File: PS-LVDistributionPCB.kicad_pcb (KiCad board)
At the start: 2 copper layers, 226 x 70 mm, 81 parts, among them J1 CRIT OUT, J10 NON CRIT OUT, J11 NON CRIT OUT, J12 NON CRIT OUT, J13 NON CRIT OUT, J14 NON CRIT OUT, J15 NON CRIT OUT, J16 NON CRIT OUT, J17 NON CRIT OUT, J18 NON CRIT OUT, J19 NON CRIT OUT, J2 CRIT OUT, J20 CRIT, J21 NON CRIT, J3 CRIT OUT, J4 CRIT OUT, J5 CRIT OUT, J6 CRIT OUT, J7 CRIT OUT, J8 NON CRIT OUT, J9 NON CRIT OUT

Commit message: Added optoisolators to ensure LED indicators are powered by critical power and only turn on when the fuse blows. Fuses and resistors on the back for waterproofing.
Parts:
- removed D1, D10, D11, D12, D13, D14, D15, D16, D17, D18, D19, D2, D3, D4, D5, D6, D7, D8, D9: 20mA, LED_SMD:LED_0805_2012Metric
- removed F1, F10, F11, F12, F13, F14, F15, F16, F17, F18, F19, F2, F3, F4, F5, F6, F7, F8, F9: 10A, footprints:3588
- removed F20, F21: 30A, footprints:3588
- removed the G*** at (216.6, 85.2)
- removed J1, J2, J3, J4, J5, J6, J7: CRIT OUT, footprints:Molex_Micro-Fit_3.0_43650-0215_1x02_P3.00mm_Vertical
- removed J10, J11, J12, J13, J14, J15, J16, J17, J18, J19, J8, J9: NON CRIT OUT, footprints:Molex_Micro-Fit_3.0_43650-0215_1x02_P3.00mm_Vertical
- removed J20: CRIT, Connector_Molex:Molex_Sabre_43160-0102_1x02_P7.49mm_Vertical
- removed J21: NON CRIT, Connector_Molex:Molex_Sabre_43160-0102_1x02_P7.49mm_Vertical
- removed R1, R10, R11, R12, R13, R14, R15, R16, R17, R18, R19, R2, R3, R4, R5, R6, R7, R8, R9: 1k, Resistor_SMD:R_0805_2012Metric
- added C_D1: 20mA, LED_SMD:LED_0805_2012Metric, F.Cu at (92.0, 89.1)
- added C_D2: 20mA, LED_SMD:LED_0805_2012Metric, F.Cu at (108.4, 89.2)
- added C_D3: 20mA, LED_SMD:LED_0805_2012Metric, F.Cu at (124.9, 89.2)
- added C_D4: 20mA, LED_SMD:LED_0805_2012Metric, F.Cu at (140.9, 89.2)
- added C_D5: 20mA, LED_SMD:LED_0805_2012Metric, F.Cu at (157.1, 89.1)
- added C_D6: 20mA, LED_SMD:LED_0805_2012Metric, F.Cu at (173.1, 89.1)
- added C_D7: 20mA, LED_SMD:LED_0805_2012Metric, F.Cu at (189.4, 89.2)
- added C_F1: 10A, footprints:3588, B.Cu at (92.0, 73.6)
- added C_F2: 10A, footprints:3588, B.Cu at (108.4, 73.6)
- added C_F3: 10A, footprints:3588, B.Cu at (124.9, 73.6)
- added C_F4: 10A, footprints:3588, B.Cu at (140.9, 73.7)
- added C_F5: 10A, footprints:3588, B.Cu at (157.1, 73.6)
- added C_F6: 10A, footprints:3588, B.Cu at (173.1, 73.6)
- added C_F7: 10A, footprints:3588, B.Cu at (189.4, 73.7)
- added C_J1: CRIT OUT, footprints:Molex_Micro-Fit_3.0_43650-0215_1x02_P3.00mm_Vertical, F.Cu at (90.5, 94.7)
- added C_J2: CRIT OUT, footprints:Molex_Micro-Fit_3.0_43650-0215_1x02_P3.00mm_Vertical, F.Cu at (106.9, 94.7)
- added C_J3: CRIT OUT, footprints:Molex_Micro-Fit_3.0_43650-0215_1x02_P3.00mm_Vertical, F.Cu at (123.4, 94.7)
- added C_J4: CRIT OUT, footprints:Molex_Micro-Fit_3.0_43650-0215_1x02_P3.00mm_Vertical, F.Cu at (139.4, 94.8)
- added C_J5: CRIT OUT, footprints:Molex_Micro-Fit_3.0_43650-0215_1x02_P3.00mm_Vertical, F.Cu at (155.6, 94.7)
- added C_J6: CRIT OUT, footprints:Molex_Micro-Fit_3.0_43650-0215_1x02_P3.00mm_Vertical, F.Cu at (171.6, 94.7)
- added C_J7: CRIT OUT, footprints:Molex_Micro-Fit_3.0_43650-0215_1x02_P3.00mm_Vertical, F.Cu at (187.9, 94.8)
- added C_R1: 105, Resistor_SMD:R_0805_2012Metric, B.Cu at (86.6, 84.7)
- added C_R10: 1k, Resistor_SMD:R_0805_2012Metric, B.Cu at (162.6, 84.6)
- added C_R11: 105, Resistor_SMD:R_0805_2012Metric, B.Cu at (167.6, 84.7)
- added C_R12: 1k, Resistor_SMD:R_0805_2012Metric, B.Cu at (178.6, 84.6)
- added C_R13: 105, Resistor_SMD:R_0805_2012Metric, B.Cu at (183.9, 84.8)
- added C_R14: 1k, Resistor_SMD:R_0805_2012Metric, B.Cu at (194.9, 84.7)
- added C_R2: 1k, Resistor_SMD:R_0805_2012Metric, B.Cu at (97.6, 84.6)
- added C_R3: 105, Resistor_SMD:R_0805_2012Metric, B.Cu at (102.9, 84.7)
- added C_R4: 1k, Resistor_SMD:R_0805_2012Metric, B.Cu at (113.9, 84.7)
- added C_R5: 105, Resistor_SMD:R_0805_2012Metric, B.Cu at (119.4, 84.7)
- added C_R6: 1k, Resistor_SMD:R_0805_2012Metric, B.Cu at (130.4, 84.7)
- added C_R7: 105, Resistor_SMD:R_0805_2012Metric, B.Cu at (135.4, 84.8)
- added C_R8: 1k, Resistor_SMD:R_0805_2012Metric, B.Cu at (146.4, 84.7)
- added C_R9: 105, Resistor_SMD:R_0805_2012Metric, B.Cu at (151.6, 84.7)
- added C_U1: EL3H7, Package_SO:SOP-4_4.4x2.6mm_P1.27mm, B.Cu at (92.0, 84.6)
- added C_U2: EL3H7, Package_SO:SOP-4_4.4x2.6mm_P1.27mm, B.Cu at (108.4, 84.7)
- added C_U3: EL3H7, Package_SO:SOP-4_4.4x2.6mm_P1.27mm, B.Cu at (124.9, 84.7)
- added C_U4: EL3H7, Package_SO:SOP-4_4.4x2.6mm_P1.27mm, B.Cu at (140.9, 84.7)
- added C_U5: EL3H7, Package_SO:SOP-4_4.4x2.6mm_P1.27mm, B.Cu at (157.1, 84.6)
- added C_U6: EL3H7, Package_SO:SOP-4_4.4x2.6mm_P1.27mm, B.Cu at (173.1, 84.6)
- added C_U7: EL3H7, Package_SO:SOP-4_4.4x2.6mm_P1.27mm, B.Cu at (189.4, 84.7)
- added G***: LOGO, UTSVT Connectors:UTSVTsmall, B.Cu at (204.6, 72.0)
- added IN_F1: 30A, footprints:3588, B.Cu at (75.6, 70.4)
- added IN_F2: 30A, footprints:3588, B.Cu at (75.6, 129.4)
- added IN_J1: CRIT, Connector_Molex:Molex_Sabre_43160-0102_1x02_P7.49mm_Vertical, B.Cu at (71.9, 91.9)
- added IN_J2: NON CRIT, Connector_Molex:Molex_Sabre_43160-0102_1x02_P7.49mm_Vertical, B.Cu at (71.9, 114.9)
- added NC_D1: 20mA, LED_SMD:LED_0805_2012Metric, F.Cu at (92.1, 110.6)
- added NC_D10: 20mA, LED_SMD:LED_0805_2012Metric, F.Cu at (238.6, 110.4)
- added NC_D11: 20mA, LED_SMD:LED_0805_2012Metric, F.Cu at (238.6, 89.4)
- added NC_D12: 20mA, LED_SMD:LED_0805_2012Metric, F.Cu at (222.1, 89.4)
- added NC_D2: 20mA, LED_SMD:LED_0805_2012Metric, F.Cu at (108.4, 110.6)
- added NC_D3: 20mA, LED_SMD:LED_0805_2012Metric, F.Cu at (124.9, 110.6)
- added NC_D4: 20mA, LED_SMD:LED_0805_2012Metric, F.Cu at (140.9, 110.6)
- added NC_D5: 20mA, LED_SMD:LED_0805_2012Metric, F.Cu at (156.9, 110.6)
- added NC_D6: 20mA, LED_SMD:LED_0805_2012Metric, F.Cu at (172.9, 110.5)
- added NC_D7: 20mA, LED_SMD:LED_0805_2012Metric, F.Cu at (189.4, 110.6)
- added NC_D8: 20mA, LED_SMD:LED_0805_2012Metric, F.Cu at (205.6, 110.3)
- added NC_D9: 20mA, LED_SMD:LED_0805_2012Metric, F.Cu at (222.1, 110.4)
- added NC_F1: 10A, footprints:3588, B.Cu at (92.0, 125.6)
- added NC_F10: 10A, footprints:3588, B.Cu at (238.5, 125.4)
- added NC_F11: 10A, footprints:3588, B.Cu at (238.6, 73.7)
- added NC_F12: 10A, footprints:3588, B.Cu at (222.1, 73.7)
- added NC_F2: 10A, footprints:3588, B.Cu at (108.4, 125.6)
- added NC_F3: 10A, footprints:3588, B.Cu at (124.9, 125.6)
- added NC_F4: 10A, footprints:3588, B.Cu at (140.9, 125.6)
- added NC_F5: 10A, footprints:3588, B.Cu at (156.9, 125.6)
- added NC_F6: 10A, footprints:3588, B.Cu at (172.9, 125.5)
- added NC_F7: 10A, footprints:3588, B.Cu at (189.4, 125.6)
- added NC_F8: 10A, footprints:3588, B.Cu at (205.5, 125.3)
- added NC_F9: 10A, footprints:3588, B.Cu at (222.1, 125.4)
- added NC_J1: NON CRIT OUT, footprints:Molex_Micro-Fit_3.0_43650-0215_1x02_P3.00mm_Vertical, F.Cu at (93.6, 105.1)
- added NC_J10: NON CRIT OUT, footprints:Molex_Micro-Fit_3.0_43650-0215_1x02_P3.00mm_Vertical, F.Cu at (240.1, 104.9)
- added NC_J11: NON CRIT OUT, footprints:Molex_Micro-Fit_3.0_43650-0215_1x02_P3.00mm_Vertical, F.Cu at (237.1, 94.9)
- added NC_J12: NON CRIT OUT, footprints:Molex_Micro-Fit_3.0_43650-0215_1x02_P3.00mm_Vertical, F.Cu at (220.6, 94.9)
- added NC_J2: NON CRIT OUT, footprints:Molex_Micro-Fit_3.0_43650-0215_1x02_P3.00mm_Vertical, F.Cu at (109.9, 105.1)
- added NC_J3: NON CRIT OUT, footprints:Molex_Micro-Fit_3.0_43650-0215_1x02_P3.00mm_Vertical, F.Cu at (126.4, 105.1)
- added NC_J4: NON CRIT OUT, footprints:Molex_Micro-Fit_3.0_43650-0215_1x02_P3.00mm_Vertical, F.Cu at (142.4, 105.1)
- added NC_J5: NON CRIT OUT, footprints:Molex_Micro-Fit_3.0_43650-0215_1x02_P3.00mm_Vertical, F.Cu at (158.4, 105.1)
- added NC_J6: NON CRIT OUT, footprints:Molex_Micro-Fit_3.0_43650-0215_1x02_P3.00mm_Vertical, F.Cu at (174.4, 105.0)
- added NC_J7: NON CRIT OUT, footprints:Molex_Micro-Fit_3.0_43650-0215_1x02_P3.00mm_Vertical, F.Cu at (190.9, 105.1)
- added NC_J8: NON CRIT OUT, footprints:Molex_Micro-Fit_3.0_43650-0215_1x02_P3.00mm_Vertical, F.Cu at (207.1, 104.8)
- added NC_J9: NON CRIT OUT, footprints:Molex_Micro-Fit_3.0_43650-0215_1x02_P3.00mm_Vertical, F.Cu at (223.6, 104.9)
- added NC_R1: 105, Resistor_SMD:R_0805_2012Metric, B.Cu at (97.6, 114.7)
- added NC_R10: 1k, Resistor_SMD:R_0805_2012Metric, B.Cu at (151.4, 114.7)
- added NC_R11: 105, Resistor_SMD:R_0805_2012Metric, B.Cu at (178.4, 114.6)
- added NC_R12: 1k, Resistor_SMD:R_0805_2012Metric, B.Cu at (167.4, 114.6)
- added NC_R13: 105, Resistor_SMD:R_0805_2012Metric, B.Cu at (194.9, 114.7)
- added NC_R14: 1k, Resistor_SMD:R_0805_2012Metric, B.Cu at (183.9, 114.7)
- added NC_R15: 105, Resistor_SMD:R_0805_2012Metric, B.Cu at (211.1, 114.4)
- added NC_R16: 1k, Resistor_SMD:R_0805_2012Metric, B.Cu at (200.1, 114.4)
- added NC_R17: 105, Resistor_SMD:R_0805_2012Metric, B.Cu at (227.6, 114.5)
- added NC_R18: 1k, Resistor_SMD:R_0805_2012Metric, B.Cu at (216.6, 114.5)
- added NC_R19: 105, Resistor_SMD:R_0805_2012Metric, B.Cu at (244.1, 114.5)
- added NC_R2: 1k, Resistor_SMD:R_0805_2012Metric, B.Cu at (86.6, 114.7)
- added NC_R20: 1k, Resistor_SMD:R_0805_2012Metric, B.Cu at (233.1, 114.5)
- added NC_R21: 105, Resistor_SMD:R_0805_2012Metric, B.Cu at (233.1, 84.7)
- added NC_R22: 1k, Resistor_SMD:R_0805_2012Metric, B.Cu at (244.1, 84.7)
- added NC_R23: 105, Resistor_SMD:R_0805_2012Metric, B.Cu at (216.6, 84.7)
- added NC_R24: 1k, Resistor_SMD:R_0805_2012Metric, B.Cu at (227.6, 84.7)
- added NC_R3: 105, Resistor_SMD:R_0805_2012Metric, B.Cu at (113.9, 114.7)
- added NC_R4: 1k, Resistor_SMD:R_0805_2012Metric, B.Cu at (102.9, 114.7)
- added NC_R5: 105, Resistor_SMD:R_0805_2012Metric, B.Cu at (130.4, 114.7)
- added NC_R6: 1k, Resistor_SMD:R_0805_2012Metric, B.Cu at (119.4, 114.7)
- added NC_R7: 105, Resistor_SMD:R_0805_2012Metric, B.Cu at (146.4, 114.7)
- added NC_R8: 1k, Resistor_SMD:R_0805_2012Metric, B.Cu at (135.4, 114.7)
- added NC_R9: 105, Resistor_SMD:R_0805_2012Metric, B.Cu at (162.4, 114.7)
- added NC_U1: EL3H7, Package_SO:SOP-4_4.4x2.6mm_P1.27mm, B.Cu at (92.1, 114.7)
- added NC_U10: EL3H7, Package_SO:SOP-4_4.4x2.6mm_P1.27mm, B.Cu at (238.6, 114.5)
- added NC_U11: EL3H7, Package_SO:SOP-4_4.4x2.6mm_P1.27mm, B.Cu at (238.6, 84.7)
- added NC_U12: EL3H7, Package_SO:SOP-4_4.4x2.6mm_P1.27mm, B.Cu at (222.1, 84.7)
- added NC_U2: EL3H7, Package_SO:SOP-4_4.4x2.6mm_P1.27mm, B.Cu at (108.4, 114.7)
- added NC_U3: EL3H7, Package_SO:SOP-4_4.4x2.6mm_P1.27mm, B.Cu at (124.9, 114.7)
- added NC_U4: EL3H7, Package_SO:SOP-4_4.4x2.6mm_P1.27mm, B.Cu at (140.9, 114.7)
- added NC_U5: EL3H7, Package_SO:SOP-4_4.4x2.6mm_P1.27mm, B.Cu at (156.9, 114.7)
- added NC_U6: EL3H7, Package_SO:SOP-4_4.4x2.6mm_P1.27mm, B.Cu at (172.9, 114.6)
- added NC_U7: EL3H7, Package_SO:SOP-4_4.4x2.6mm_P1.27mm, B.Cu at (189.4, 114.7)
- added NC_U8: EL3H7, Package_SO:SOP-4_4.4x2.6mm_P1.27mm, B.Cu at (205.6, 114.4)
- added NC_U9: EL3H7, Package_SO:SOP-4_4.4x2.6mm_P1.27mm, B.Cu at (222.1, 114.5)
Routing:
- net GND: track 0.00 -> 178.5 mm, vias 0 -> 19
- net +12V_NON: track 72.7 -> 7.36 mm
- net +12V CRIT: track 42.4 -> 0.00 mm
- net Net-(NC_D10-A): track 0.00 -> 13.1 mm, vias 0 -> 1
- net Net-(NC_D9-A): track 0.00 -> 13.1 mm, vias 0 -> 1
- net Net-(NC_D7-A): track 0.00 -> 13.1 mm, vias 0 -> 1
- net Net-(NC_D6-A): track 0.00 -> 13.1 mm, vias 0 -> 1
- net Net-(NC_D5-A): track 0.00 -> 13.1 mm, vias 0 -> 1
- net Net-(NC_D2-A): track 0.00 -> 13.1 mm, vias 0 -> 1
- net Net-(NC_D8-A): track 0.00 -> 13.1 mm, vias 0 -> 1
- net Net-(NC_D4-A): track 0.00 -> 13.1 mm, vias 0 -> 1
- net Net-(NC_D3-A): track 0.00 -> 13.1 mm, vias 0 -> 1
- net Net-(NC_D12-A): track 0.00 -> 7.27 mm, vias 0 -> 1
- net Net-(NC_D11-A): track 0.00 -> 7.27 mm, vias 0 -> 1
- net Net-(C_D6-A): track 0.00 -> 7.25 mm, vias 0 -> 1
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- added copper zone on B.Cu, net Net-(C_J1-Pin_1)
- added copper zone on B.Cu, net Net-(C_J2-Pin_1)
- added copper zone on B.Cu, net Net-(C_J3-Pin_1)
- added copper zone on B.Cu, net Net-(C_J4-Pin_1)
- added copper zone on B.Cu, net Net-(C_J5-Pin_1)
- added copper zone on B.Cu, net Net-(C_J6-Pin_1)
- added copper zone on B.Cu, net Net-(C_J7-Pin_1)
- added copper zone on B.Cu, net Net-(IN_J1-Pin_1)
- added copper zone on B.Cu, net Net-(IN_J2-Pin_1)
- added copper zone on B.Cu, net Net-(NC_J1-Pin_1)
- added copper zone on B.Cu, net Net-(NC_J10-Pin_1)
- added copper zone on B.Cu, net Net-(NC_J11-Pin_1)
- added copper zone on B.Cu, net Net-(NC_J12-Pin_1)
- added copper zone on B.Cu, net Net-(NC_J2-Pin_1)
- added copper zone on B.Cu, net Net-(NC_J3-Pin_1)
- added copper zone on B.Cu, net Net-(NC_J4-Pin_1)
- added copper zone on B.Cu, net Net-(NC_J5-Pin_1)
- added copper zone on B.Cu, net Net-(NC_J6-Pin_1)
- added copper zone on B.Cu, net Net-(NC_J7-Pin_1)
- added copper zone on B.Cu, net Net-(NC_J8-Pin_1)
- added copper zone on B.Cu, net Net-(NC_J9-Pin_1)
- removed copper zone on B.Cu, net Net-(J1-Pin_1)
- removed copper zone on B.Cu, net Net-(J10-Pin_1)
- removed copper zone on B.Cu, net Net-(J11-Pin_1)
- removed copper zone on B.Cu, net Net-(J12-Pin_1)
- removed copper zone on B.Cu, net Net-(J13-Pin_1)
- removed copper zone on B.Cu, net Net-(J14-Pin_1)
- removed copper zone on B.Cu, net Net-(J15-Pin_1)
- removed copper zone on B.Cu, net Net-(J16-Pin_1)
- removed copper zone on B.Cu, net Net-(J17-Pin_1)
- removed copper zone on B.Cu, net Net-(J18-Pin_1)
- removed copper zone on B.Cu, net Net-(J19-Pin_1)
- removed copper zone on B.Cu, net Net-(J2-Pin_1)
- removed copper zone on B.Cu, net Net-(J20-Pin_1)
- removed copper zone on B.Cu, net Net-(J21-Pin_1)
- removed copper zone on B.Cu, net Net-(J3-Pin_1)
- removed copper zone on B.Cu, net Net-(J4-Pin_1)
- removed copper zone on B.Cu, net Net-(J5-Pin_1)
- removed copper zone on B.Cu, net Net-(J6-Pin_1)
- removed copper zone on B.Cu, net Net-(J7-Pin_1)
- removed copper zone on B.Cu, net Net-(J8-Pin_1)
- removed copper zone on B.Cu, net Net-(J9-Pin_1)
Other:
- board size 226 x 70 mm -> 191.9 x 83.9 mm
- board text added: "LV Distribution Surabhi Karighattam 2024"
- board text added: "NON CRIT 1"
- board text added: "NON CRIT 10"
- board text added: "NON CRIT 11"
- board text added: "NON CRIT 12"
- board text added: "NON CRIT 2"
- board text added: "NON CRIT 3"
- board text added: "NON CRIT 4"
- board text added: "NON CRIT 5"
- board text added: "NON CRIT 6"
- board text added: "NON CRIT 7"
- board text added: "NON CRIT 8"
- board text added: "NON CRIT 9"
- board text added: "NON CRIT IN"
- board text removed: "LV Distribution Surabhi Karighattam 2025"
- board text removed: "NC 1"
- board text removed: "NC 10"
- board text removed: "NC 11"
- board text removed: "NC 12"
- board text removed: "NC 2"
- board text removed: "NC 3"
- board text removed: "NC 4"
- board text removed: "NC 5"
- board text removed: "NC 6"
- board text removed: "NC 7"
- board text removed: "NC 8"
- board text removed: "NC 9"
- board text removed: "NC IN"

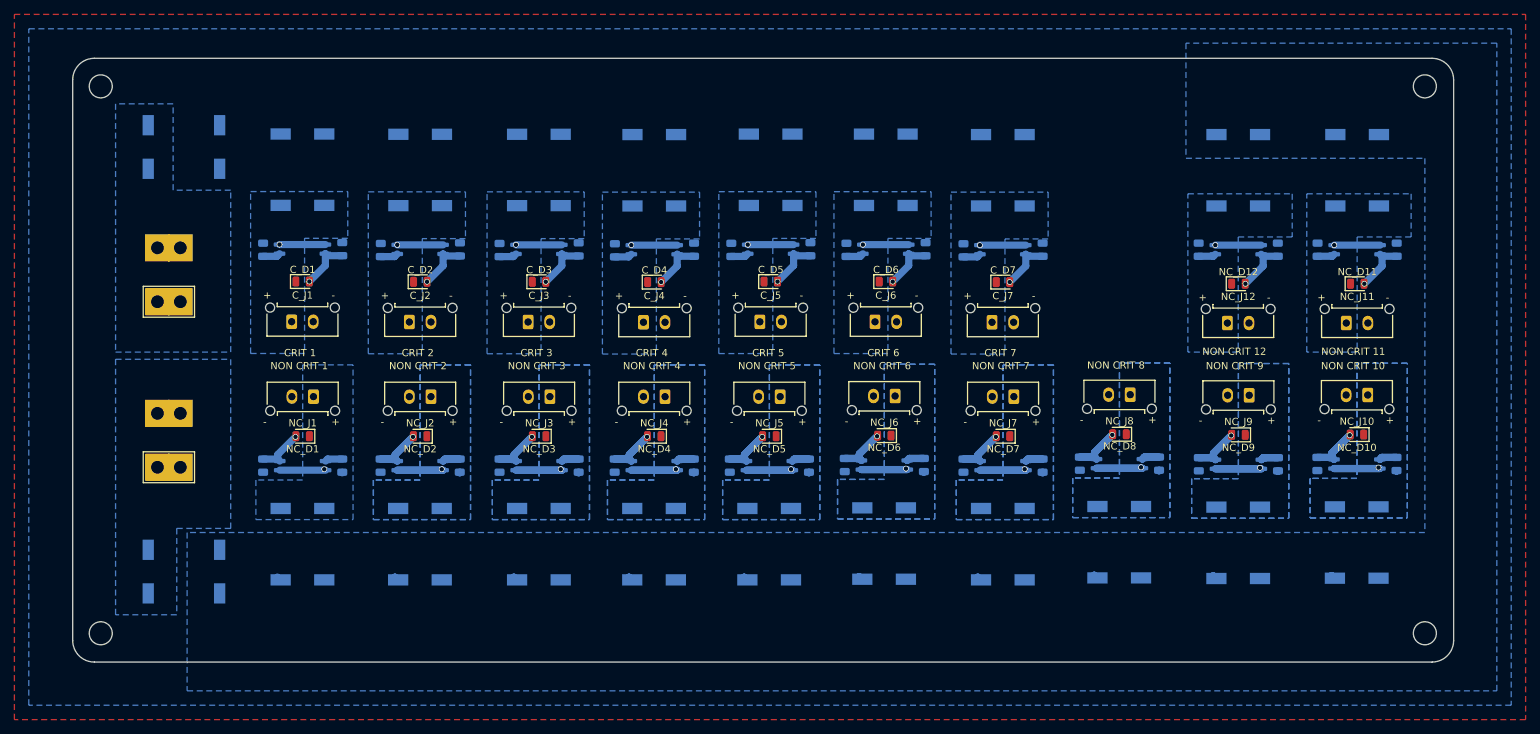
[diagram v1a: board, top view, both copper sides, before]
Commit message: xt30s + right angle mx150 initial layout
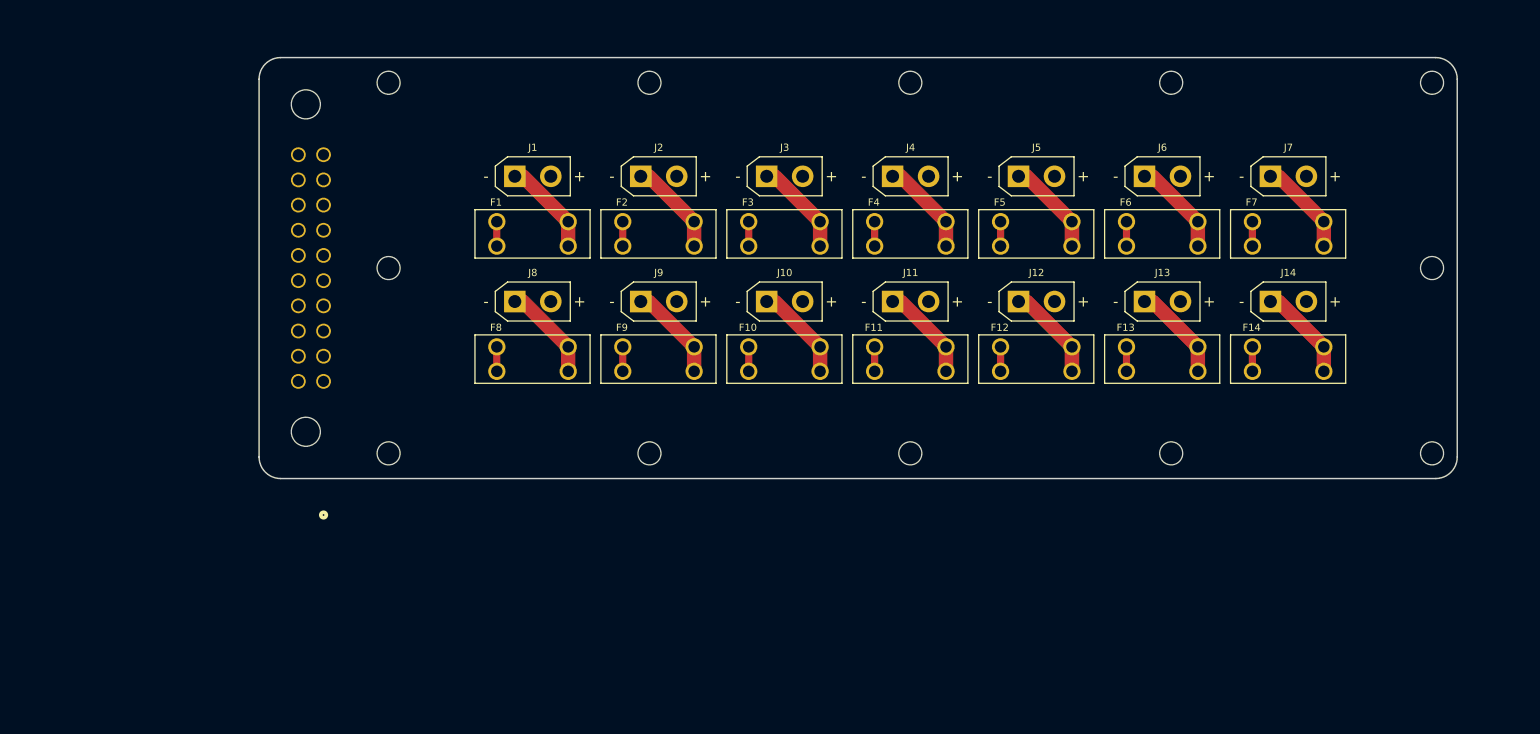
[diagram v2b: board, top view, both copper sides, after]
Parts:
- removed C_D1, C_D2, C_D3, C_D4, C_D5, C_D6, C_D7, NC_D1, NC_D10, NC_D11, NC_D12, NC_D2, NC_D3, NC_D4, NC_D5, NC_D6, NC_D7, NC_D8, NC_D9: 20mA, LED_SMD:LED_0805_2012Metric
- removed C_F1, C_F2, C_F3, C_F4, C_F5, C_F6, C_F7, NC_F1, NC_F10, NC_F11, NC_F12, NC_F2, NC_F3, NC_F4, NC_F5, NC_F6, NC_F7, NC_F8, NC_F9: 10A, footprints:3588
- removed C_J1, C_J2, C_J3, C_J4, C_J5, C_J6, C_J7: CRIT OUT, footprints:Molex_Micro-Fit_3.0_43650-0215_1x02_P3.00mm_Vertical
- removed C_R1, C_R11, C_R13, C_R3, C_R5, C_R7, C_R9, NC_R1, NC_R11, NC_R13, NC_R15, NC_R17, NC_R19, NC_R21, NC_R23, NC_R3, NC_R5, NC_R7, NC_R9: 105, Resistor_SMD:R_0805_2012Metric
- removed C_R10, C_R12, C_R14, C_R2, C_R4, C_R6, C_R8, NC_R10, NC_R12, NC_R14, NC_R16, NC_R18, NC_R2, NC_R20, NC_R22, NC_R24, NC_R4, NC_R6, NC_R8: 1k, Resistor_SMD:R_0805_2012Metric
- removed C_U1, C_U2, C_U3, C_U4, C_U5, C_U6, C_U7, NC_U1, NC_U10, NC_U11, NC_U12, NC_U2, NC_U3, NC_U4, NC_U5, NC_U6, NC_U7, NC_U8, NC_U9: EL3H7, Package_SO:SOP-4_4.4x2.6mm_P1.27mm
- removed G***: LOGO, UTSVT Connectors:UTSVTsmall
- removed IN_F1, IN_F2: 30A, footprints:3588
- removed IN_J1: CRIT, Connector_Molex:Molex_Sabre_43160-0102_1x02_P7.49mm_Vertical
- removed IN_J2: NON CRIT, Connector_Molex:Molex_Sabre_43160-0102_1x02_P7.49mm_Vertical
- removed NC_J1, NC_J10, NC_J11, NC_J12, NC_J2, NC_J3, NC_J4, NC_J5, NC_J6, NC_J7, NC_J8, NC_J9: NON CRIT OUT, footprints:Molex_Micro-Fit_3.0_43650-0215_1x02_P3.00mm_Vertical
- added F1: 3568, footprints:FUSE_3568, F.Cu at (124.0, 82.5)
- added F10: 3568, footprints:FUSE_3568, F.Cu at (159.0, 99.9)
- added F11: 3568, footprints:FUSE_3568, F.Cu at (176.5, 99.9)
- added F12: 3568, footprints:FUSE_3568, F.Cu at (194.0, 99.9)
- added F13: 3568, footprints:FUSE_3568, F.Cu at (211.5, 99.9)
- added F14: 3568, footprints:FUSE_3568, F.Cu at (229.0, 99.9)
- added F2: 3568, footprints:FUSE_3568, F.Cu at (141.5, 82.5)
- added F3: 3568, footprints:FUSE_3568, F.Cu at (159.0, 82.5)
- added F4: 3568, footprints:FUSE_3568, F.Cu at (176.5, 82.5)
- added F5: 3568, footprints:FUSE_3568, F.Cu at (194.0, 82.5)
- added F6: 3568, footprints:FUSE_3568, F.Cu at (211.5, 82.5)
- added F7: 3568, footprints:FUSE_3568, F.Cu at (229.0, 82.5)
- added F8: 3568, footprints:FUSE_3568, F.Cu at (124.0, 99.9)
- added F9: 3568, footprints:FUSE_3568, F.Cu at (141.5, 99.9)
- added J1: Conn_01x02, footprints:AMASS_XT30UPB-M_1x02_P5.0mm_Vertical, F.Cu at (121.5, 74.5)
- added J10: Conn_01x02, footprints:AMASS_XT30UPB-M_1x02_P5.0mm_Vertical, F.Cu at (156.5, 91.9)
- added J11: Conn_01x02, footprints:AMASS_XT30UPB-M_1x02_P5.0mm_Vertical, F.Cu at (174.0, 91.9)
- added J12: Conn_01x02, footprints:AMASS_XT30UPB-M_1x02_P5.0mm_Vertical, F.Cu at (191.5, 91.9)
- added J13: Conn_01x02, footprints:AMASS_XT30UPB-M_1x02_P5.0mm_Vertical, F.Cu at (209.0, 91.9)
- added J14: Conn_01x02, footprints:AMASS_XT30UPB-M_1x02_P5.0mm_Vertical, F.Cu at (226.5, 91.9)
- added J15: Conn_01x20, footprints:CONN_SD-34829-001_20_ST_MOL, B.Cu at (95.0, 103.0)
- added J2: Conn_01x02, footprints:AMASS_XT30UPB-M_1x02_P5.0mm_Vertical, F.Cu at (139.0, 74.5)
- added J3: Conn_01x02, footprints:AMASS_XT30UPB-M_1x02_P5.0mm_Vertical, F.Cu at (156.5, 74.5)
- added J4: Conn_01x02, footprints:AMASS_XT30UPB-M_1x02_P5.0mm_Vertical, F.Cu at (174.0, 74.5)
- added J5: Conn_01x02, footprints:AMASS_XT30UPB-M_1x02_P5.0mm_Vertical, F.Cu at (191.5, 74.5)
- added J6: Conn_01x02, footprints:AMASS_XT30UPB-M_1x02_P5.0mm_Vertical, F.Cu at (209.0, 74.5)
- added J7: Conn_01x02, footprints:AMASS_XT30UPB-M_1x02_P5.0mm_Vertical, F.Cu at (226.5, 74.5)
- added J8: Conn_01x02, footprints:AMASS_XT30UPB-M_1x02_P5.0mm_Vertical, F.Cu at (121.5, 91.9)
- added J9: Conn_01x02, footprints:AMASS_XT30UPB-M_1x02_P5.0mm_Vertical, F.Cu at (139.0, 91.9)
- added REF**: MountingHole_3.2mm_M3, MountingHole:MountingHole_3.2mm_M3, F.Cu at (104.0, 87.2)
- added REF**: MountingHole_3.2mm_M3, MountingHole:MountingHole_3.2mm_M3, F.Cu at (140.2, 61.5)
- added REF**: MountingHole_3.2mm_M3, MountingHole:MountingHole_3.2mm_M3, F.Cu at (249.0, 61.5)
- added REF**: MountingHole_3.2mm_M3, MountingHole:MountingHole_3.2mm_M3, F.Cu at (176.5, 61.5)
- added REF**: MountingHole_3.2mm_M3, MountingHole:MountingHole_3.2mm_M3, F.Cu at (249.0, 87.2)
- added REF**: MountingHole_3.2mm_M3, MountingHole:MountingHole_3.2mm_M3, F.Cu at (176.5, 113.0)
- added REF**: MountingHole_3.2mm_M3, MountingHole:MountingHole_3.2mm_M3, F.Cu at (104.0, 61.5)
- added REF**: MountingHole_3.2mm_M3, MountingHole:MountingHole_3.2mm_M3, F.Cu at (212.8, 113.0)
- added REF**: MountingHole_3.2mm_M3, MountingHole:MountingHole_3.2mm_M3, F.Cu at (212.8, 61.5)
- added REF**: MountingHole_3.2mm_M3, MountingHole:MountingHole_3.2mm_M3, F.Cu at (140.2, 113.0)
- added REF**: MountingHole_3.2mm_M3, MountingHole:MountingHole_3.2mm_M3, F.Cu at (104.0, 113.0)
- added REF**: MountingHole_3.2mm_M3, MountingHole:MountingHole_3.2mm_M3, F.Cu at (249.0, 113.0)
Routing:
- net GND: track 178.5 -> 0.00 mm, vias 19 -> 0
- net Net-(J7-Pin_1): track 0.00 -> 13.4 mm
- net Net-(J6-Pin_1): track 0.00 -> 13.4 mm
- net Net-(J5-Pin_1): track 0.00 -> 13.4 mm
- net Net-(J4-Pin_1): track 0.00 -> 13.4 mm
- net Net-(J3-Pin_1): track 0.00 -> 13.4 mm
- net Net-(J2-Pin_1): track 0.00 -> 13.4 mm
- net Net-(J9-Pin_1): track 0.00 -> 13.4 mm
- net Net-(J14-Pin_1): track 0.00 -> 13.4 mm
- net Net-(J13-Pin_1): track 0.00 -> 13.4 mm
- net Net-(J12-Pin_1): track 0.00 -> 13.4 mm
- net Net-(J11-Pin_1): track 0.00 -> 13.4 mm
- net Net-(J10-Pin_1): track 0.00 -> 13.4 mm
- net Net-(J1-Pin_1): track 0.00 -> 13.4 mm
- net Net-(J8-Pin_1): track 0.00 -> 13.4 mm
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- removed copper zone on B.Cu, net +12V CRIT
- removed copper zone on B.Cu, net +12V_NON
- removed copper zone on F.Cu, net GND
- removed copper zone on B.Cu, net Net-(C_J1-Pin_1)
- removed copper zone on B.Cu, net Net-(C_J2-Pin_1)
- removed copper zone on B.Cu, net Net-(C_J3-Pin_1)
- removed copper zone on B.Cu, net Net-(C_J4-Pin_1)
- removed copper zone on B.Cu, net Net-(C_J5-Pin_1)
- removed copper zone on B.Cu, net Net-(C_J6-Pin_1)
- removed copper zone on B.Cu, net Net-(C_J7-Pin_1)
- removed copper zone on B.Cu, net Net-(IN_J1-Pin_1)
- removed copper zone on B.Cu, net Net-(IN_J2-Pin_1)
- removed copper zone on B.Cu, net Net-(NC_J1-Pin_1)
- removed copper zone on B.Cu, net Net-(NC_J10-Pin_1)
- removed copper zone on B.Cu, net Net-(NC_J11-Pin_1)
- removed copper zone on B.Cu, net Net-(NC_J12-Pin_1)
- removed copper zone on B.Cu, net Net-(NC_J2-Pin_1)
- removed copper zone on B.Cu, net Net-(NC_J3-Pin_1)
- removed copper zone on B.Cu, net Net-(NC_J4-Pin_1)
- removed copper zone on B.Cu, net Net-(NC_J5-Pin_1)
- removed copper zone on B.Cu, net Net-(NC_J6-Pin_1)
- removed copper zone on B.Cu, net Net-(NC_J7-Pin_1)
- removed copper zone on B.Cu, net Net-(NC_J8-Pin_1)
- removed copper zone on B.Cu, net Net-(NC_J9-Pin_1)
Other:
- board size 191.9 x 83.9 mm -> 166.5 x 58.5 mm
- board text removed: "+"
- board text removed: "-"
- board text removed: "CRIT 1"
- board text removed: "CRIT 2"
- board text removed: "CRIT 3"
- board text removed: "CRIT 4"
- board text removed: "CRIT 5"
- board text removed: "CRIT 6"
- board text removed: "CRIT 7"
- board text removed: "CRIT IN"
- board text removed: "LV Distribution Surabhi Karighattam 2024"
- board text removed: "NON CRIT 1"
- board text removed: "NON CRIT 10"
- board text removed: "NON CRIT 11"
- board text removed: "NON CRIT 12"
- board text removed: "NON CRIT 2"
- board text removed: "NON CRIT 3"
- board text removed: "NON CRIT 4"
- board text removed: "NON CRIT 5"
- board text removed: "NON CRIT 6"
- board text removed: "NON CRIT 7"
- board text removed: "NON CRIT 8"
- board text removed: "NON CRIT 9"
- board text removed: "NON CRIT IN"

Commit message: common gnd
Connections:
- J1 pad 2: GND1 -> GND
- J10 pad 2: GND4 -> GND
- J11 pad 2: GND5 -> GND
- J12 pad 2: GND5 -> GND
- J13 pad 2: GND6 -> GND
- J14 pad 2: GND6 -> GND
- J15 pad 15: GND1 -> GND
- J15 pad 16: GND2 -> GND
- J15 pad 17: GND3 -> GND
- J15 pad 18: GND4 -> GND
- J15 pad 19: GND5 -> GND
- J15 pad 20: GND6 -> GND
- J2 pad 2: GND1 -> GND
- J3 pad 2: GND1 -> GND
- J4 pad 2: GND2 -> GND
- J5 pad 2: GND2 -> GND
- J6 pad 2: GND3 -> GND
- J7 pad 2: GND3 -> GND
- J8 pad 2: GND3 -> GND
- J9 pad 2: GND4 -> GND
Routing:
- added copper zone on B.Cu, net GND
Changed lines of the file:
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@@
 	(net 26 "P13")
 	(net 27 "P14")
-	(net 28 "GND6")
-	(net 29 "GND3")
-	(net 30 "GND2")
-	(net 31 "GND1")
-	(net 32 "GND5")
-	(net 33 "GND4")
-	(net 34 "Net-(J1-Pin_1)")
+	(net 28 "GND")
+	(net 29 "Net-(J1-Pin_1)")
 	(footprint "MountingHole:MountingHole_3.2mm_M3"
 		(layer "F.Cu")
@@
 			(layers "*.Cu" "*.Mask")
 			(remove_unused_layers no)
-			(net 30 "GND2")
+			(net 28 "GND")
 			(pinfunction "Pin_2")
 			(pintype "passive")
@@
 			(layers "*.Cu" "*.Mask")
 			(remove_unused_layers no)
-			(net 32 "GND5")
+			(net 28 "GND")
 			(pinfunction "Pin_2")
 			(pintype "passive")
@@
 			(layers "*.Cu" "*.Mask")
 			(remove_unused_layers no)
-			(net 34 "Net-(J1-Pin_1)")
+			(net 29 "Net-(J1-Pin_1)")
 			(pinfunction "Pin_1")
 			(pintype "passive")
@@
 			(layers "*.Cu" "*.Mask")
 			(remove_unused_layers no)
-			(net 31 "GND1")
+			(net 28 "GND")
 			(pinfunction "Pin_2")
 			(pintype "passive")
@@
 			(layers "*.Cu" "*.Mask")
 			(remove_unused_layers no)
-			(net 33 "GND4")
+			(net 28 "GND")
 			(pinfunction "Pin_2")
 			(pintype "passive")
@@
 			(layers "*.Cu" "*.Mask")
 			(remove_unused_layers no)
-			(net 29 "GND3")
+			(net 28 "GND")
 			(pinfunction "Pin_2")
 			(pintype "passive")
@@
 			(layers "*.Cu" "*.Mask")
 			(remove_unused_layers no)
-			(net 30 "GND2")
+			(net 28 "GND")
 			(pinfunction "Pin_2")
 			(pintype "passive")
@@
 			(layers "*.Cu" "*.Mask")
 			(remove_unused_layers no)
-			(net 28 "GND6")
+			(net 28 "GND")
 			(pinfunction "Pin_2")
 			(pintype "passive")
@@
 			(layers "*.Cu" "*.Mask")
 			(remove_unused_layers no)
-			(net 28 "GND6")
+			(net 28 "GND")
 			(pinfunction "Pin_2")
 			(pintype "passive")
@@
 			(layers "*.Cu" "*.Mask")
 			(remove_unused_layers no)
-			(net 33 "GND4")
+			(net 28 "GND")
 			(pinfunction "Pin_2")
 			(pintype "passive")
@@
 			(layers "*.Cu" "*.Mask")
 			(remove_unused_layers no)
-			(net 31 "GND1")
+			(net 28 "GND")
 			(pinfunction "Pin_2")
 			(pintype "passive")
@@
 			(layers "*.Cu" "*.Mask")
 			(remove_unused_layers no)
-			(net 34 "Net-(J1-Pin_1)")
+			(net 29 "Net-(J1-Pin_1)")
 			(pintype "passive")
 			(solder_mask_margin 0.102)
@@
 			(layers "*.Cu" "*.Mask")
 			(remove_unused_layers no)
-			(net 34 "Net-(J1-Pin_1)")
+			(net 29 "Net-(J1-Pin_1)")
 			(pintype "passive")
 			(solder_mask_margin 0.102)
@@
 			(layers "*.Cu" "*.Mask")
 			(remove_unused_layers no)
-			(net 32 "GND5")
+			(net 28 "GND")
 			(pinfunction "Pin_2")
 			(pintype "passive")
@@
 			(layers "*.Cu" "*.Mask")
 			(remove_unused_layers no)
-			(net 29 "GND3")
+			(net 28 "GND")
 			(pinfunction "Pin_2")
 			(pintype "passive")
@@
 			(layers "*.Cu" "*.Mask")
 			(remove_unused_layers no)
-			(net 29 "GND3")
+			(net 28 "GND")
 			(pinfunction "Pin_2")
 			(pintype "passive")
@@
 			(layers "*.Cu" "*.Mask")
 			(remove_unused_layers no)
-			(net 31 "GND1")
+			(net 28 "GND")
 			(pinfunction "Pin_2")
 			(pintype "passive")
@@
 			(layers "*.Cu" "*.Mask")
 			(remove_unused_layers no)
-			(net 31 "GND1")
+			(net 28 "GND")
 			(pinfunction "Pin_15")
 			(pintype "passive")
@@
 			(layers "*.Cu" "*.Mask")
 			(remove_unused_layers no)
-			(net 30 "GND2")
+			(net 28 "GND")
 			(pinfunction "Pin_16")
 			(pintype "passive")
@@
 			(layers "*.Cu" "*.Mask")
 			(remove_unused_layers no)
-			(net 29 "GND3")
+			(net 28 "GND")
 			(pinfunction "Pin_17")
 			(pintype "passive")
@@
 			(layers "*.Cu" "*.Mask")
 			(remove_unused_layers no)
-			(net 33 "GND4")
+			(net 28 "GND")
 			(pinfunction "Pin_18")
 			(pintype "passive")
@@
 			(layers "*.Cu" "*.Mask")
 			(remove_unused_layers no)
-			(net 32 "GND5")
+			(net 28 "GND")
 			(pinfunction "Pin_19")
 			(pintype "passive")
@@
 			(layers "*.Cu" "*.Mask")
 			(remove_unused_layers no)
-			(net 28 "GND6")
+			(net 28 "GND")
 			(pinfunction "Pin_20")
 			(pintype "passive")
@@
 		(width 1)
 		(layer "F.Cu")
-		(net 34)
+		(net 29)
 	)
 	(segment
@@
 		(width 2)
 		(layer "F.Cu")
-		(net 34)
+		(net 29)
 	)
 	(segment
@@
 		(width 2)
 		(layer "F.Cu")
-		(net 34)
+		(net 29)
+	)
+	(zone
+		(net 28)
+		(net_name "GND")
+		(layer "B.Cu")
+		(hatch edge 0.5)
+		(connect_pads yes
+			(clearance 0.5)
+		)
+		(min_thickness 0.25)
+		(filled_areas_thickness no)
+		(fill yes
+			(thermal_gap 0.5)
+			(thermal_bridge_width 0.5)
+		)
+		(polygon
+			(pts
+				(xy 86 58) (xy 86 116.5) (xy 253 116.5) (xy 253 58)
+			)
+		)
 	)
 	(group "Replicated Group ['/Power Output5/']"
